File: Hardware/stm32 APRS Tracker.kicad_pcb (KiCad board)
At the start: 2 copper layers, 113 parts, among them IC1 STM32F103x, P1 USB_B, P101 CONN_01X04, P102 CONN_01X04, P103 CONN_01X01, P201 CONN_01X02, P301 CONN_01X06, P302 CONN_01X06, P303 CONN_01X08, P304 CONN_01X08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

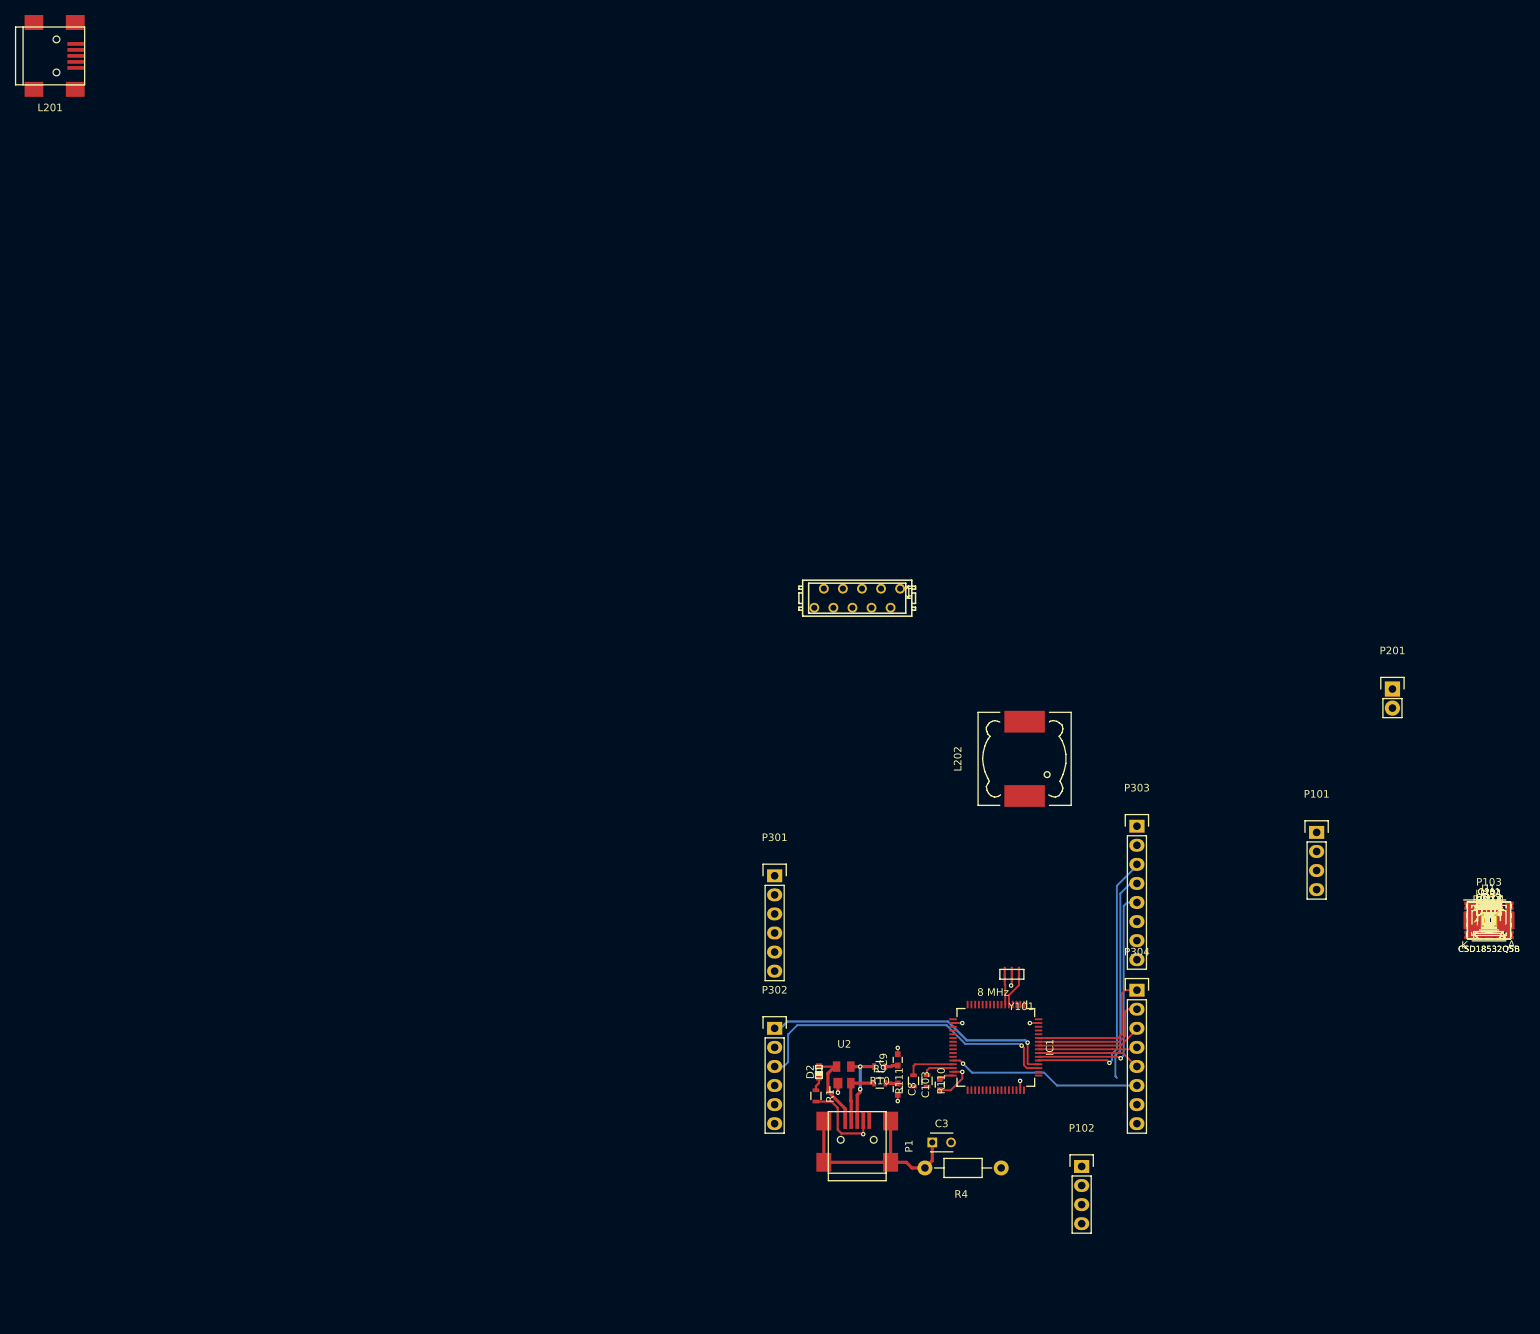
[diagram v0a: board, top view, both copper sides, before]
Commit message: Schaltwandler fast fertig
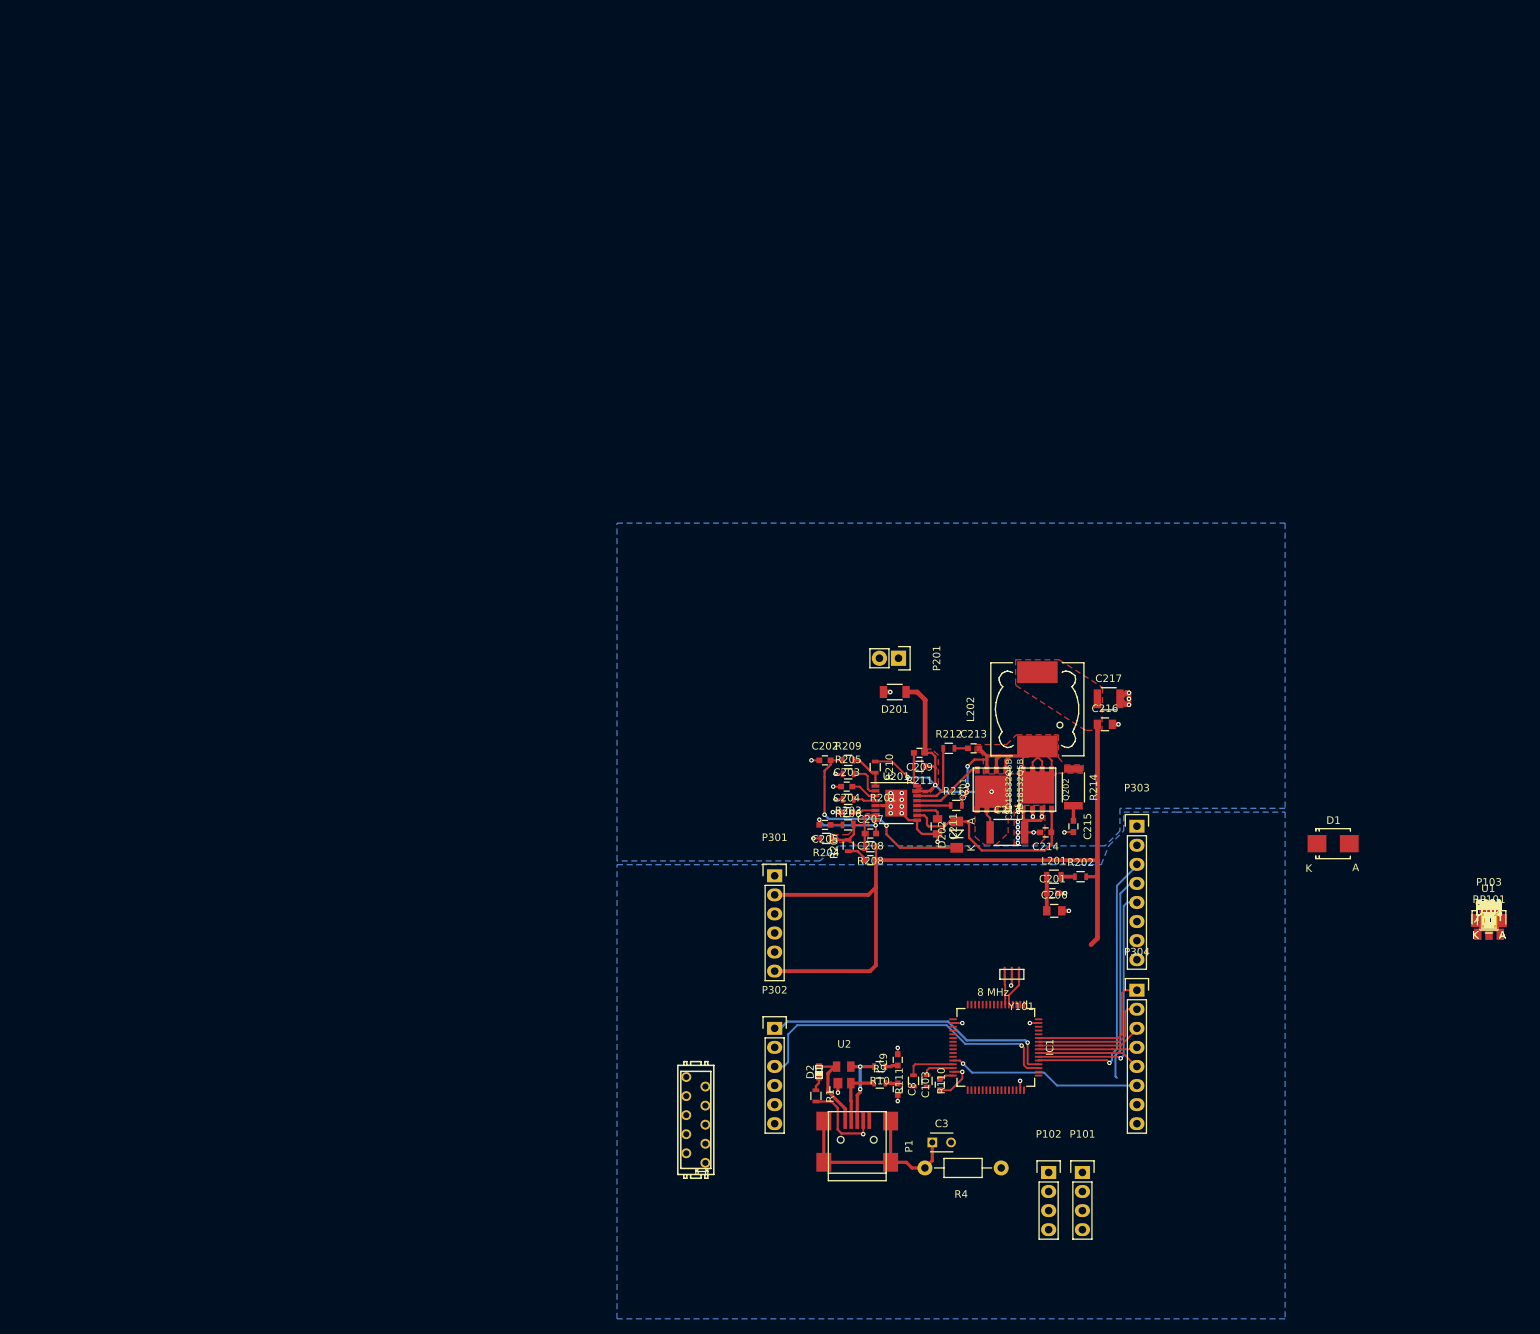
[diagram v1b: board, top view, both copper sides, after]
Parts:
- L201: footprint Connect:USB_Mini-B -> Resistors_SMD:R_0805
- Q201, Q202: footprint PhilippsFootprints:SON5x6_FET -> PhilippsFootprints:SON5x6_FET_123
- R201: footprint Resistors_SMD:R_0603 -> mw_inductor
- moved L201 172.7 mm to (133.7, 109.3)
- moved C202 91.0 mm to (103.2, 93.8)
- moved C205 89.4 mm to (103.2, 102.4), turned to 180 degrees
- moved R204 89.0 mm to (103.4, 104.2), turned to 180 degrees
- moved R209 88.0 mm to (106.3, 93.8)
- moved R205 87.6 mm to (106.3, 95.6)
- moved C203 87.4 mm to (106.1, 97.3)
- moved R206 86.9 mm to (106.3, 99.0), turned to 180 degrees
- moved C204 86.8 mm to (106.1, 100.7)
- moved R203 86.3 mm to (106.3, 102.4)
- moved R207 85.9 mm to (106.3, 105.2), turned to 90 degrees
- moved D201 84.8 mm to (112.5, 84.7), turned to 180 degrees
- moved R210 84.3 mm to (109.9, 94.7), turned to 270 degrees
- moved C207 83.2 mm to (109.3, 103.6)
- moved R208 83.0 mm to (109.3, 105.3), turned to 180 degrees
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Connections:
- C111 pad 1: (no net) -> Net-(C111-Pad1)
- C207 pad 1: Net-(C205-Pad2) -> Net-(C207-Pad1)
- C208 pad 2: /Power/Vout -> +3V3
- D1 pad 2: (no net) -> Net-(D1-Pad2)
- IC1 pad 2: (no net) -> Net-(IC1-Pad2)
- IC1 pad 21: (no net) -> /SPI1_SCK
- IC1 pad 22: (no net) -> /SPI1_MISO
- IC1 pad 23: (no net) -> /SPI1_MOSI
- IC1 pad 37: (no net) -> /Tast0
- IC1 pad 50: (no net) -> /Squelch
- IC1 pad 9: (no net) -> /HfPowerDown
- P103 pad 1: (no net) -> Net-(L104-Pad2)
- P201 pad 1: (no net) -> Net-(F201-Pad1)
- P302 pad 6: (no net) -> Net-(P302-Pad6)
- P303 pad 1: (no net) -> Net-(P303-Pad1)
- P303 pad 2: (no net) -> Net-(P303-Pad2)
- P304 pad 7: (no net) -> Net-(P304-Pad7)
- P304 pad 8: (no net) -> Net-(P304-Pad8)
- R109 pad 1: (no net) -> Net-(DRA101-Pad5)
- R113 pad 1: (no net) -> Net-(DRA101-Pad16)
- R114 pad 2: (no net) -> Net-(DRA101-Pad17)
- R203 pad 2: Net-(R203-Pad2) -> Net-(C207-Pad1)
- R204 pad 1: Net-(R203-Pad2) -> Net-(C207-Pad1)
- R207 pad 2: Net-(R203-Pad2) -> Net-(C207-Pad1)
- R208 pad 1: /Power/Vout -> +3V3
- R208 pad 2: Net-(R203-Pad2) -> Net-(C207-Pad1)
- R215 pad 2: (no net) -> GNDPWR
- U101 pad 2: (no net) -> Net-(U101-Pad2)
- U101 pad 4: (no net) -> Net-(U101-Pad4)
- U101 pad 6: (no net) -> Net-(U101-Pad6)
- U201 pad 13: (no net) -> Net-(Q201-Pad2)
- U201 pad 7: Net-(R203-Pad2) -> Net-(C207-Pad1)
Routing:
- net +3V3: track 1.95 -> 106.5 mm
- net Akku: track 0.00 -> 53.0 mm, vias 0 -> 3
- net GNDREF: track 0.00 -> 47.5 mm, vias 0 -> 30
- net Net-(C213-Pad2): track 0.00 -> 40.6 mm, vias 0 -> 2
- net Net-(C202-Pad2): track 0.00 -> 29.3 mm, vias 0 -> 2
- net Net-(C214-Pad1): track 0.00 -> 27.4 mm
- net Net-(C207-Pad1): track 0.00 -> 11.6 mm
- net Net-(C205-Pad2): track 0.00 -> 11.1 mm, vias 0 -> 2
- net Net-(Q201-Pad2): track 0.00 -> 9.72 mm
- net Net-(R212-Pad1): track 0.00 -> 9.29 mm
- net Net-(R209-Pad2): track 0.00 -> 5.32 mm
- net Net-(R205-Pad2): track 0.00 -> 4.81 mm
- net Net-(C209-Pad2): track 0.00 -> 4.63 mm
- net VAA: track 0.00 -> 4.55 mm
- net Net-(R213-Pad1): track 0.00 -> 4.49 mm
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- added copper zone on F.Cu, net +3V3
- added copper zone on F.Cu, net Akku
- added copper zone on B.Cu, net GND
- added copper zone on B.Cu, net GNDREF
- added copper zone on F.Cu, net GNDREF
- added copper zone on F.Cu, net Net-(C207-Pad1)
- added copper zone on F.Cu, net Net-(C213-Pad2)

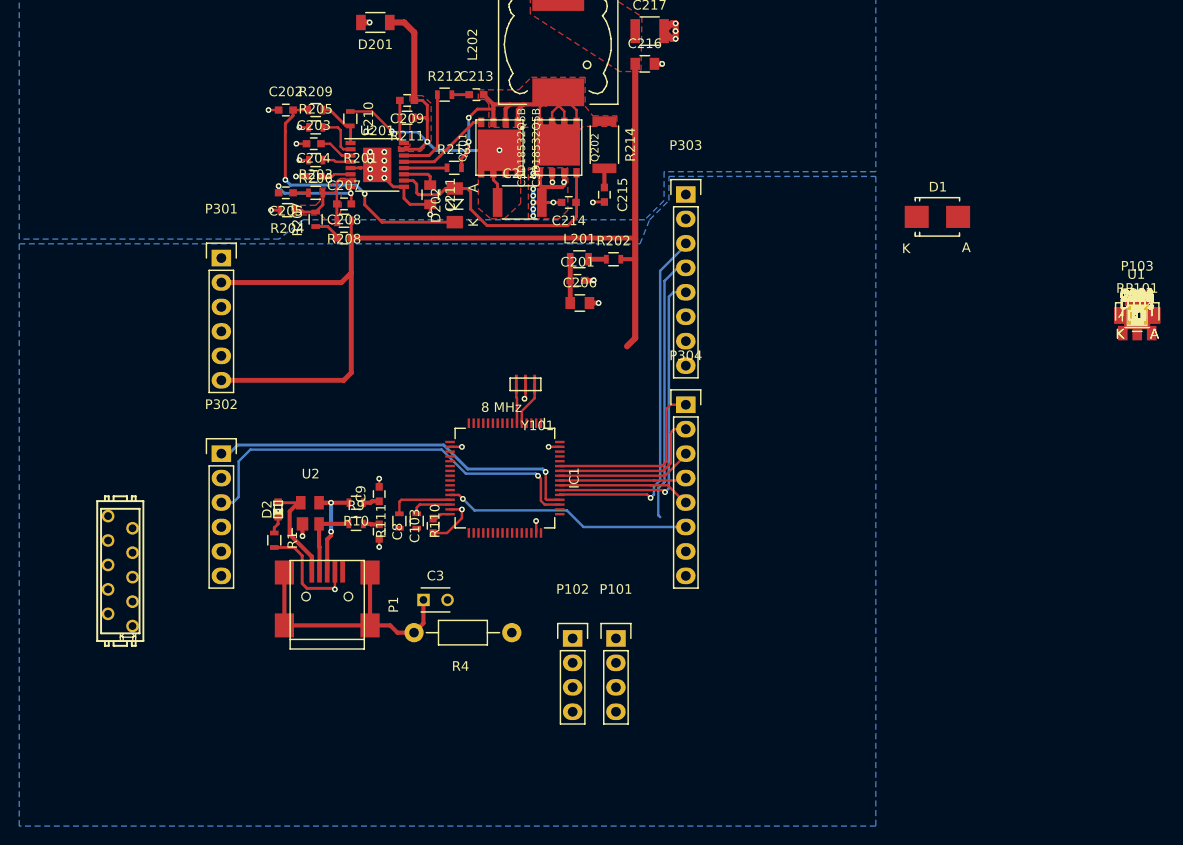
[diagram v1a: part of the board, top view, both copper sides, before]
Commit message: Layout durchaus weiter, STM fast komplett angeschlossen
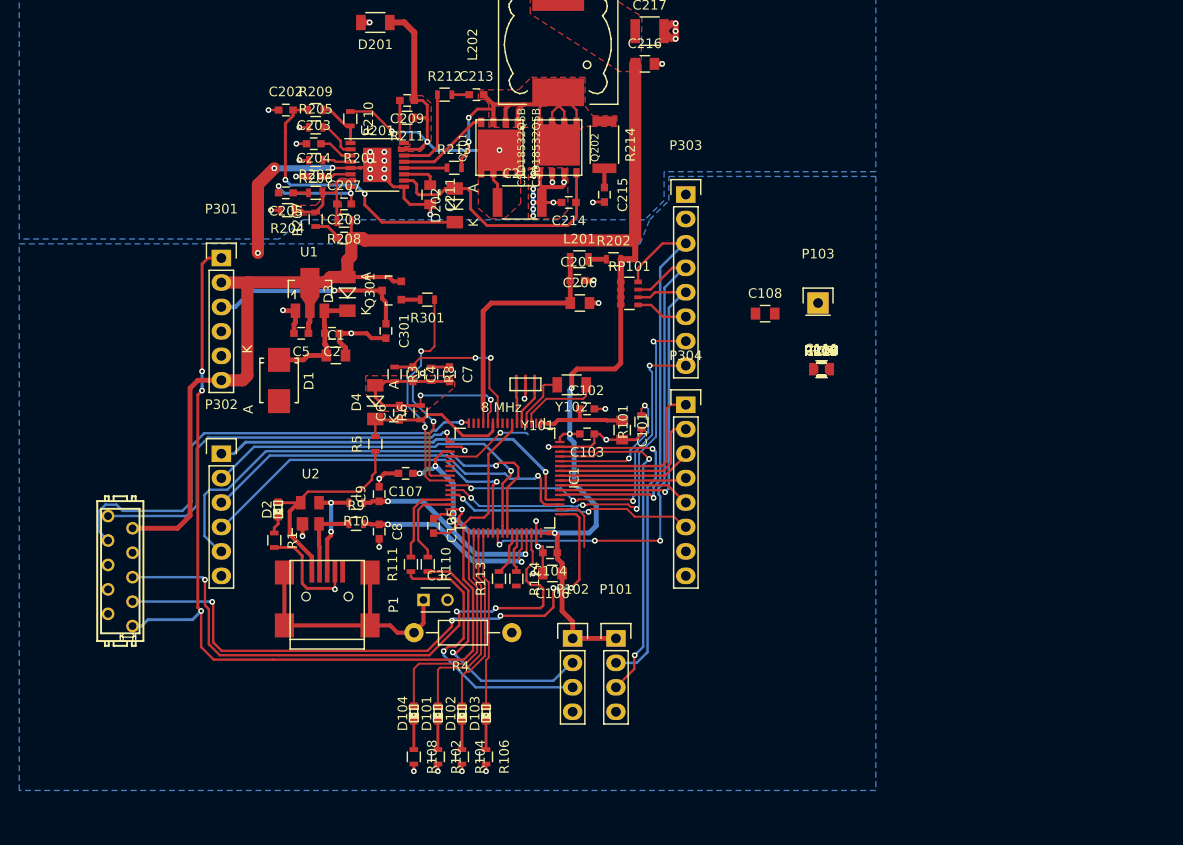
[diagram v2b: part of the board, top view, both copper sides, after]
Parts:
- moved R108 88.1 mm to (116.5, 161.0), turned to 270 degrees
- moved C5 86.9 mm to (104.8, 117.0), turned to 180 degrees
- moved U1 86.0 mm to (105.7, 112.8)
- moved R102 85.9 mm to (119.0, 161.0), turned to 270 degrees
- moved D104 85.8 mm to (116.5, 156.5), turned to 90 degrees
- moved R104 83.8 mm to (121.5, 161.0), turned to 270 degrees
- moved C2 83.7 mm to (108.0, 117.0), turned to 180 degrees
- moved D101 83.6 mm to (119.0, 156.5), turned to 90 degrees
- moved C1 83.4 mm to (108.4, 119.3)
- moved D3 82.1 mm to (109.6, 112.9), turned to 90 degrees
- moved R106 81.7 mm to (124.0, 161.0), turned to 270 degrees
- moved D102 81.5 mm to (121.5, 156.5), turned to 90 degrees
- moved R5 80.3 mm to (112.5, 128.5), turned to 90 degrees
- moved D4 79.7 mm to (112.5, 124.2), turned to 90 degrees
- moved D103 79.3 mm to (124.0, 156.5), turned to 90 degrees
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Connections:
- RP101 pad 5: /320x240 LCD Module/SD_MISO -> /320x240 LCD Module/SD_CS
- RP101 pad 7: /320x240 LCD Module/SD_SCK -> /320x240 LCD Module/SD_MISO
- RP101 pad 8: /320x240 LCD Module/SD_CS -> /320x240 LCD Module/SD_SCK
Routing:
- net +3V3: track 106.5 -> 271.0 mm, vias 0 -> 6
- net /320x240 LCD Module/Reset: track 0.00 -> 106.3 mm, vias 0 -> 3
- net /SwClk: track 0.00 -> 64.2 mm, vias 0 -> 5
- net /SwDio: track 0.00 -> 62.2 mm, vias 0 -> 3
- net GND: track 28.4 -> 87.7 mm, vias 11 -> 24
- net /uart2tx: track 0.00 -> 49.7 mm, vias 0 -> 1
- net /320x240 LCD Module/Rst: track 0.00 -> 49.4 mm, vias 0 -> 1
- net /uart2rx: track 0.00 -> 43.4 mm, vias 0 -> 1
- net /320x240 LCD Module/D1: track 0.00 -> 42.1 mm, vias 0 -> 4
- net /320x240 LCD Module/WR: track 0.00 -> 39.5 mm, vias 0 -> 1
- net /320x240 LCD Module/D0: track 0.00 -> 38.4 mm, vias 0 -> 4
- net /320x240 LCD Module/CS: track 0.00 -> 37.9 mm, vias 0 -> 1
- net /I2C1_SDA: track 0.00 -> 35.2 mm, vias 0 -> 1
- net /I2C1_SCL: track 0.00 -> 35.0 mm, vias 0 -> 2
- net Net-(P102-Pad3): track 0.00 -> 29.3 mm, vias 0 -> 1
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- added copper zone on F.Cu, net GNDA
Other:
- board text added: "KEINE BAUTEILE"

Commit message: platine fast fertig.
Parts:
- added D5: STPS340U, Diodes_SMD:Diode-SMB_Standard, F.Cu at (106.5, 85.2)
- added D6: STPS340U, Diodes_SMD:Diode-SMB_Standard, F.Cu at (100.0, 85.2)
- added DRA101: DRA818V, PhilippsFootprints:DRA8x8, F.Cu at (80.0, 102.9)
- added P2: CONN_01X02, Pin_Headers:Pin_Header_Straight_1x02, F.Cu at (106.5, 79.2)
- added SW101: SW_TxPwr, library_toni:Button_SMD_Schurter_LSG, F.Cu at (93.6, 157.8)
- R4: value 22 -> 1M
- moved C108 86.7 mm to (73.2, 81.0), turned to 90 degrees
- moved R109 80.8 mm to (78.2, 123.7)
- moved C111 80.4 mm to (79.0, 129.4)
- moved R116 77.3 mm to (82.2, 130.9), turned to 270 degrees
- moved R115 77.0 mm to (82.2, 127.9), turned to 270 degrees
- moved C210 60.0 mm to (106.2, 91.9), turned to 180 degrees
- moved R11 45.0 mm to (115.7, 133.4), turned to 180 degrees
- moved C112 39.0 mm to (121.1, 110.9)
- moved R117 38.4 mm to (121.1, 113.5), turned to 180 degrees
- moved R2 35.0 mm to (125.5, 110.1), turned to 270 degrees
- moved R103 32.1 mm to (137.7, 144.9), turned to 180 degrees
- moved R107 30.5 mm to (137.7, 142.8)
- moved R105 30.3 mm to (128.8, 117.8)
- moved R7 30.1 mm to (128.8, 119.7), turned to 180 degrees
- moved P201 13.0 mm to (100.0, 79.2), turned to 180 degrees
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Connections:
- D1 pad 2: Net-(D1-Pad2) -> +5V
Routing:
- net Net-(DRA101-Pad16): track 0.00 -> 106.5 mm, vias 0 -> 6
- net /TXPower: track 0.00 -> 104.0 mm, vias 0 -> 4
- net Net-(DRA101-Pad17): track 0.00 -> 103.5 mm, vias 0 -> 4
- net /Squelch: track 6.09 -> 104.3 mm, vias 0 -> 8
- net /HfPowerDown: track 0.00 -> 96.3 mm, vias 0 -> 4
- net +3V3: track 271.0 -> 330.7 mm
- net /Tast0: track 0.00 -> 56.9 mm, vias 0 -> 4
- net /analogIn: track 0.00 -> 54.4 mm, vias 0 -> 6
- net /PTT: track 0.00 -> 49.4 mm, vias 0 -> 4
- net VAA: track 25.6 -> 68.8 mm, vias 0 -> 2
- net Net-(C112-Pad1): track 0.00 -> 36.1 mm, vias 0 -> 2
- net Net-(DRA101-Pad5): track 0.00 -> 31.7 mm, vias 0 -> 2
- net Net-(C111-Pad1): track 0.00 -> 27.3 mm
- net GND: track 87.7 -> 107.9 mm, vias 24 -> 32
- net /DAC1: track 9.20 -> 23.5 mm, vias 1 -> 2
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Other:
- board outline added: 83 x 92.5 mm
- board text added: "Outline des LCD-Moduls. keine Platinenaußenline!"

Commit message: Platine bis auf Sicherung fertig
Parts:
- removed R215: 0*, Resistors_SMD:R_0603
- added BT101: CR2032, Pin_Headers:Pin_Header_Angled_1x02, F.Cu at (130.6, 76.9)
- added C109: 30p, Capacitors_SMD:C_0402, F.Cu at (91.5, 83.2)
- added C110: 30p, Capacitors_SMD:C_0402, F.Cu at (88.8, 81.5)
- added L101: 56nH, Capacitors_SMD:C_0402, F.Cu at (92.0, 86.2)
- added L102: 100nH, Capacitors_SMD:C_0402, F.Cu at (91.5, 80.9)
- added L103: 56nH, Capacitors_SMD:C_0402, F.Cu at (86.6, 80.4)
- added P3: CONN_01X01, Mounting_Holes:MountingHole_3mm, F.Cu at (71.5, 158.7)
- added P4: CONN_01X01, Mounting_Holes:MountingHole_3mm, F.Cu at (143.5, 158.7)
- added P5: CONN_01X01, Mounting_Holes:MountingHole_3mm, F.Cu at (80.0, 77.2)
- added P6: CONN_01X01, Mounting_Holes:MountingHole_3mm, F.Cu at (143.0, 77.2)
- moved P103 78.8 mm to (89.5, 75.7)
- moved R216 49.5 mm to (109.5, 123.7)
- moved R201 0.16 mm to (111.4, 99.9)
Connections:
- R216 pad 1: GNDREF -> GND
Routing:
- net +BATT: track 9.80 -> 80.5 mm
- net GND: track 107.9 -> 170.2 mm, vias 32 -> 38
- net (no net): track 0.00 -> 6.60 mm, vias 0 -> 2
- net Net-(L103-Pad2): track 0.00 -> 6.38 mm
- net Net-(DRA101-Pad12): track 0.00 -> 5.22 mm
- net Net-(C109-Pad1): track 0.00 -> 4.75 mm
- net Net-(C110-Pad1): track 0.00 -> 4.30 mm
- net GNDA: track 25.0 -> 27.3 mm
- net /320x240 LCD Module/WR: track 39.5 -> 40.9 mm
